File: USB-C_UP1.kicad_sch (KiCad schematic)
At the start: 21 parts, among them J12 USB_C_Receptacle, J13 I2C_HD3SS3220, U26 HD3SS3220IRNHR, U27 TPD4E02B04DQA, U28 TPD4E02B04DQA, U29 TPD4E02B04DQA

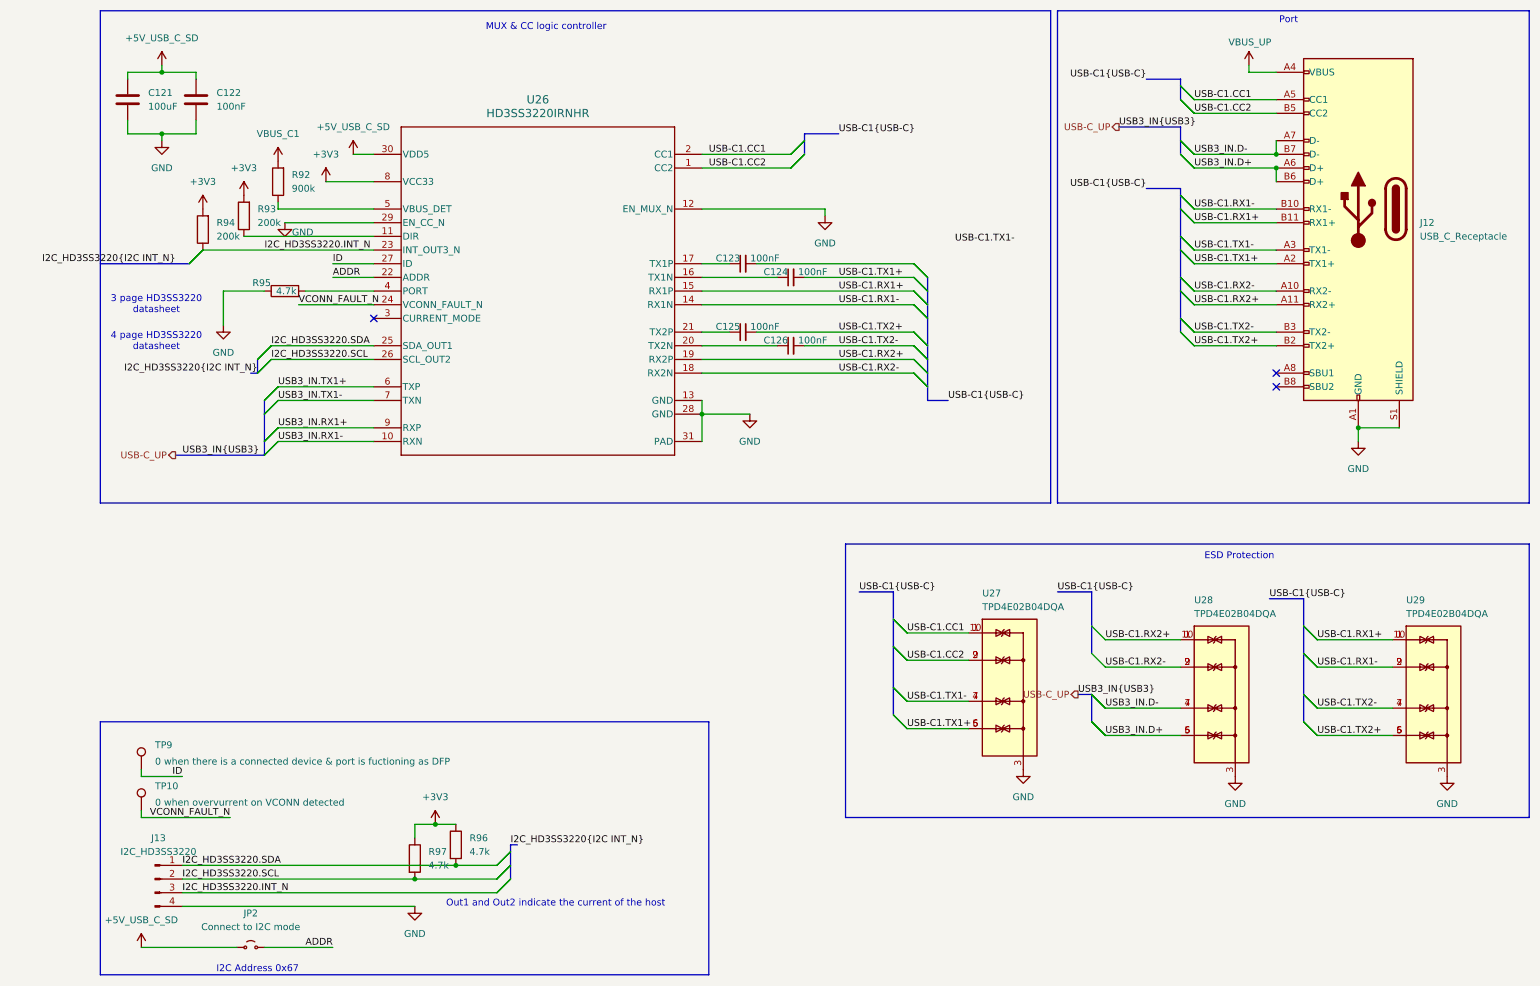
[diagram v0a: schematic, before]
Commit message: Design rule file added, lots of minor tweaks, routing done (including differential pairs), DRC done/
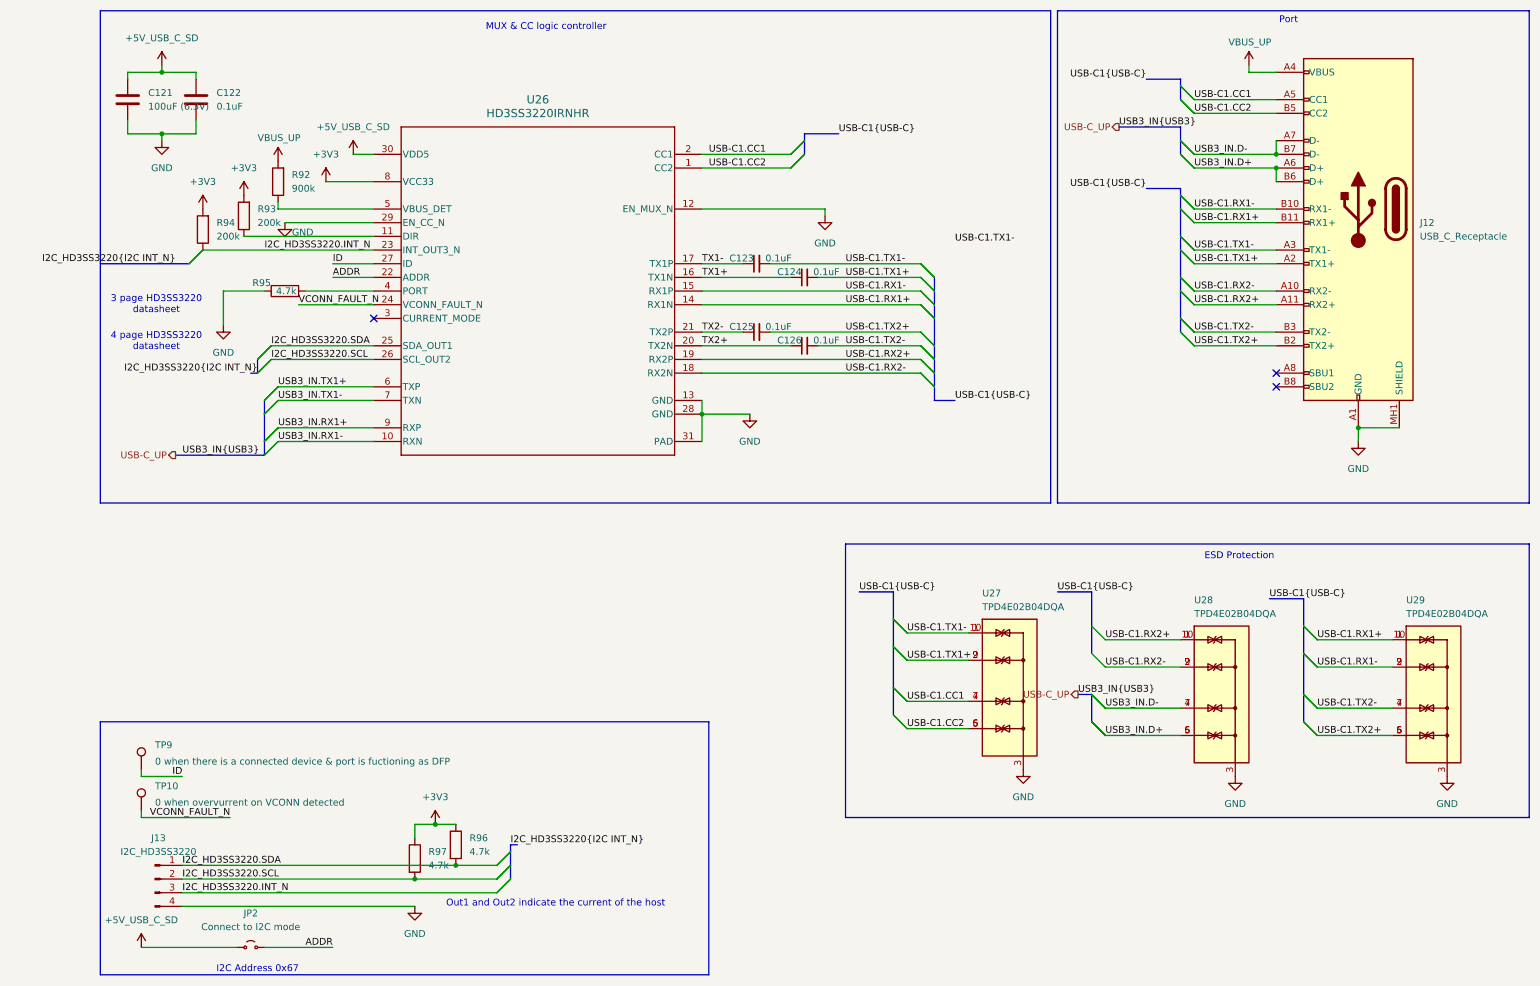
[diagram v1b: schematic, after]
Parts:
- C121: value 100uF -> 100uF (6.3V); LCSC Part C141660 -> C141660
- C122, C123, C124, C125, C126: value 100nF -> 0.1uF; LCSC Part C181043 -> C181043
- J12: footprint Connector_USB:USB_C_Receptacle_Amphenol_12401610E4-2A -> SamacSys_Parts:DX07S024XJ1R1100; LCSC Part (none) -> C134113
- J13: footprint Connector_PinHeader_1.00mm:PinHeader_1x03_P1.00mm_Vertical -> Connector_PinHeader_1.00mm:PinHeader_1x04_P1.00mm_Vertical; now left out of the parts list
- JP2, TP10, TP9: now left out of the parts list
- R92: Mouser Part No  603-RT1206CRE07900KL -> 603-RT1206CRE07900KL
- R93, R94: LCSC Part C25764 -> C25764
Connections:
- net VBUS_C1 is gone; now on net VBUS_UP: R92.2
- net GND: now also J12.MH1 (SHIELD), J12.MH2 (SHIELD), J12.MH3 (SHIELD), J12.MH4 (SHIELD); no longer J12.S1 (SHIELD)
- net USB-C1.CC1: now also U27.4 (IO3), U27.7 (NC); no longer U27.1 (IO1), U27.10 (NC)
- net USB-C1.CC2: now also U27.5 (IO4), U27.6 (NC); no longer U27.2 (IO2), U27.9 (NC)
- net USB-C1.RX1+: now also U26.14 (RX1N); no longer U26.15 (RX1P)
- net USB-C1.RX1-: now also U26.15 (RX1P); no longer U26.14 (RX1N)
- net USB-C1.TX1+: now also U27.2 (IO2), U27.9 (NC); no longer U27.5 (IO4), U27.6 (NC)
- net USB-C1.TX1-: now also C123.2, U27.1 (IO1), U27.10 (NC); no longer U27.4 (IO3), U27.7 (NC)
- net TX1+: now reaches C124.1, U26.16 (TX1N)
- net TX1-: now reaches C123.1, U26.17 (TX1P)
- net TX2+: now reaches C126.1, U26.20 (TX2N)
- net TX2-: now reaches C125.1, U26.21 (TX2P)
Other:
- company: (none) -> Karol Woźniak
- moved on the sheet: C123, C124, C125, C126
